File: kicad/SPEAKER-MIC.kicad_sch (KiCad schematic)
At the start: 23 parts, among them J018 SPEAKER1, J18 SPEAKER2, U16 8002D1

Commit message: Added Pi CM4/CM5
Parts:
- removed C16: 1uF, oomwoo_altium:C0402, symbol *:SPEAKER-MIC_0_mirrored_CAP NP_*
- removed C17: 100pF, oomwoo_altium:C0402, symbol *:SPEAKER-MIC_0_CAP NP_*
- removed C5, C93: 0.22uF, oomwoo_altium:CAP-0603, symbol DesignLibrary:SPEAKER-MIC_0_Capacitor-1_DesignLibrary.SchLib
- removed ED1, ED2: ESD5451N, oomwoo_altium:ESD0402, symbol *:SPEAKER-MIC_3_DIODE BI_DIR TRIG_*
- removed MIC1: MIC-4020, oomwoo_altium:MIC-SMD_BD4.0-4013_SMDA, symbol *:SPEAKER-MIC_0_MIC_*
- removed R118, R35: 22K, oomwoo_altium:RES-0402, symbol DesignLibrary:SPEAKER-MIC_0_Resistor-1_DesignLibrary.SchLib
- removed R119: 10K, oomwoo_altium:RES-0402, symbol DesignLibrary:SPEAKER-MIC_1_Resistor-1_DesignLibrary.SchLib
- removed R19: 100R, Resistor_SMD:R_0402_1005Metric, symbol *:SPEAKER-MIC_1_RESISTOR5_*
- removed R21, R22: 1.1K, Resistor_SMD:R_0402_1005Metric, symbol *:SPEAKER-MIC_0_RESISTOR5_*
- added C5: C_Small, symbol Device:C_Small
- added C6, C8: 33n, symbol Device:C_Small
- added C7, C9: 10u, symbol Device:C_Small
- added Q21: RTR030N05HZGTL, LIB_RTR030N05HZGTL:SOT95P280X100-3N, symbol SamacSys_Parts:RTR030N05HZGTL
- added R12, R9: 0, symbol Device:R_US
- added R13, R8: 100k, symbol Device:R_US
- added R2, R6: 270, symbol Device:R_US
- added R5, R7: 150, symbol Device:R_US
- added U11: MAX98357AETE_T, JLCImport:MAX98357AETE_T, symbol JLCImport:MAX98357AETE_T
- added U9: ICS-43434_C5656610, JLCImport:ICS-43434_C5656610, symbol JLCImport:ICS-43434_C5656610
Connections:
- net AUDIO-HP-L: now also R6.1
- net AUDIO-HP-R: now also R2.1
- net GND: now also C5.2, C6.2, C8.2, Q21.2 (S), R12.1, R5.1, R7.1, R8.2, U11.11 (GND), U11.15 (GND), U11.17 (EP), U11.3 (GND), U9.2 (LR), U9.3 (GND)
- net at R36.2, U16.3 (+IN): now also C7.2
- net at R117.1, U16.4 (-IN): now also C9.2
- net AUDIO-SD renamed SP_SHUTDOWN
- net SP_SHUTDOWN: now also Q21.1 (G), R13.2
- net SPK_N: no longer names the net of ED3.1, J18.1
- net SPK_N: now also U11.10 (OUTN)
- net SPK_P: no longer names the net of ED4.1, J18.2
- net SPK_P: now also U11.9 (OUTP)
- net VCC-5V-SYS renamed VCC-5V-REG
- net VCC-5V-REG: now also U11.8 (VDD)
- new net: R12.2, U11.2 (GAIN_SLOT)
- new net: C8.1, C9.1, R6.2, R7.2
- new net: C6.1, C7.1, R2.2, R5.2
- new net: Q21.3 (D), R9.1
- new net: R9.2, U11.4 (SD_MODE#)
- new net BCLK: U11.16 (BCLK), U9.4 (SCK)
- new net DIN: U11.1 (DIN)
- new net DOUT: R8.1, U9.6 (SD)
- new net LRCLK: U11.14 (LRCLK), U9.1 (WS)
- new net VCC3V3_SYS: C5.1, R13.1, U9.5 (VDD)
- no-connect marks 3 -> 5
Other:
- note added: "12dB"
- note added: "LEFT CHANNEL SELECT"
- note added: "Microphone Input"
- note removed: "Microphone Input(Differential)"
- moved on the sheet: C94, C95, ED3, ED4, J018, J18, L3, R117, R36, U16

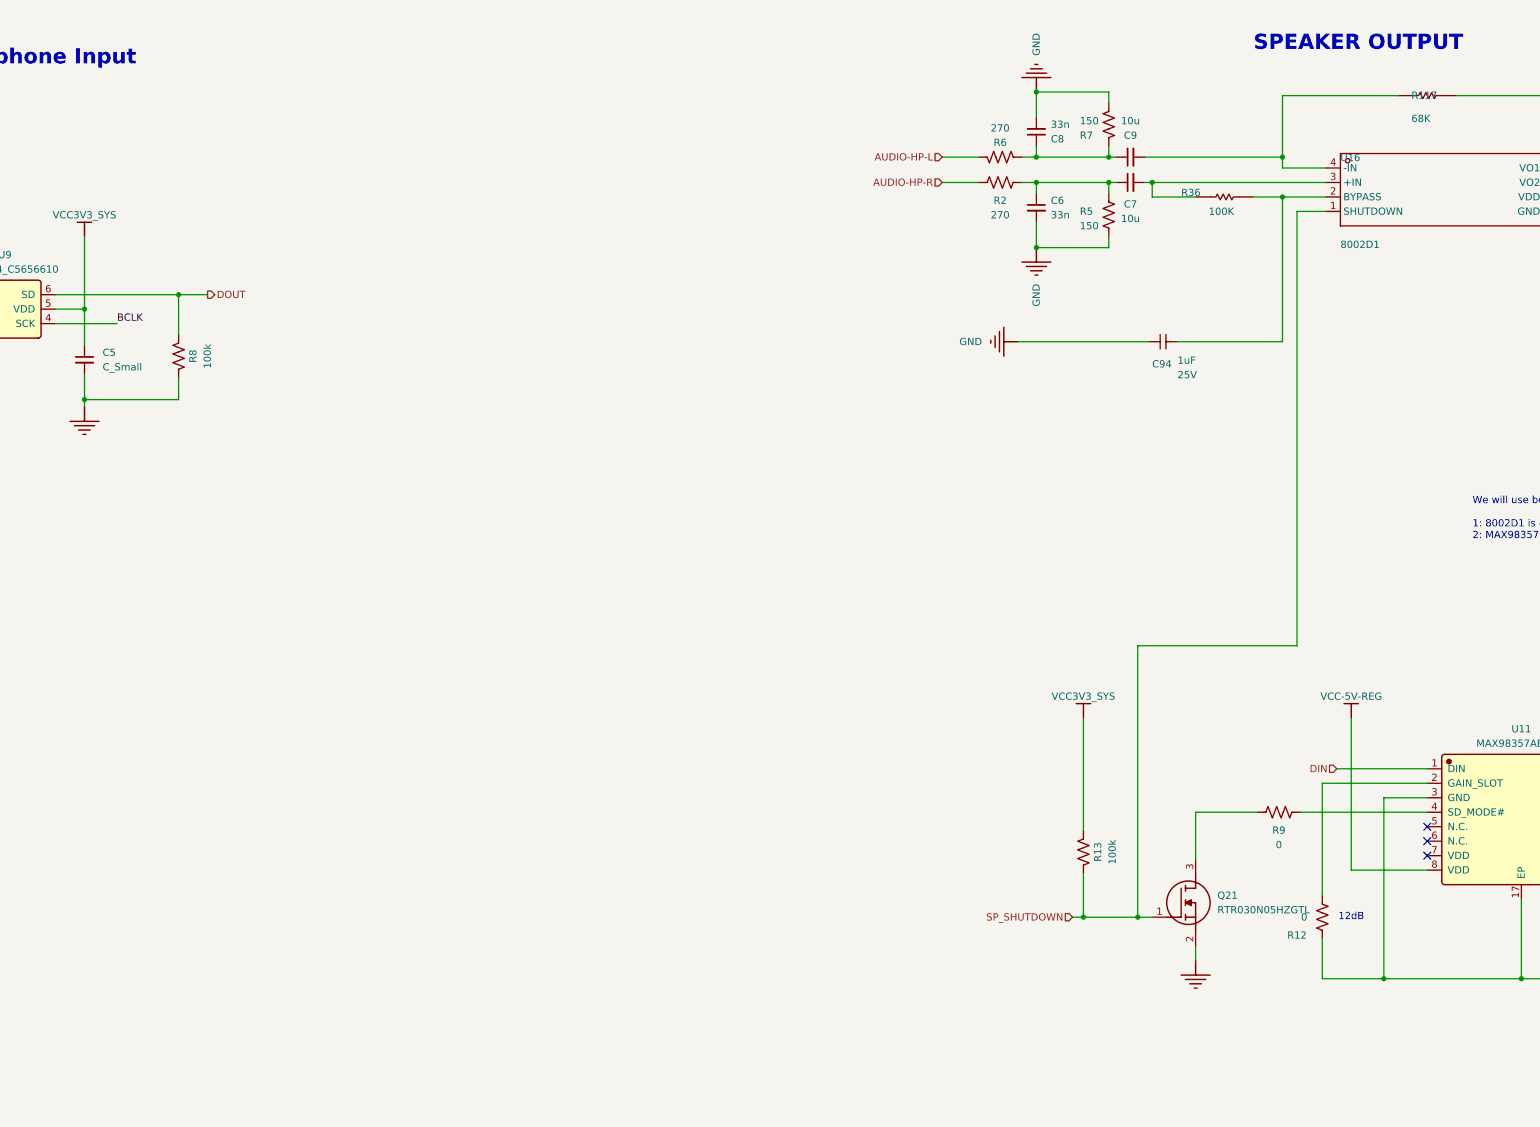
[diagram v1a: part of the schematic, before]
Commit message: Changed MCU to STM32G473VCT6
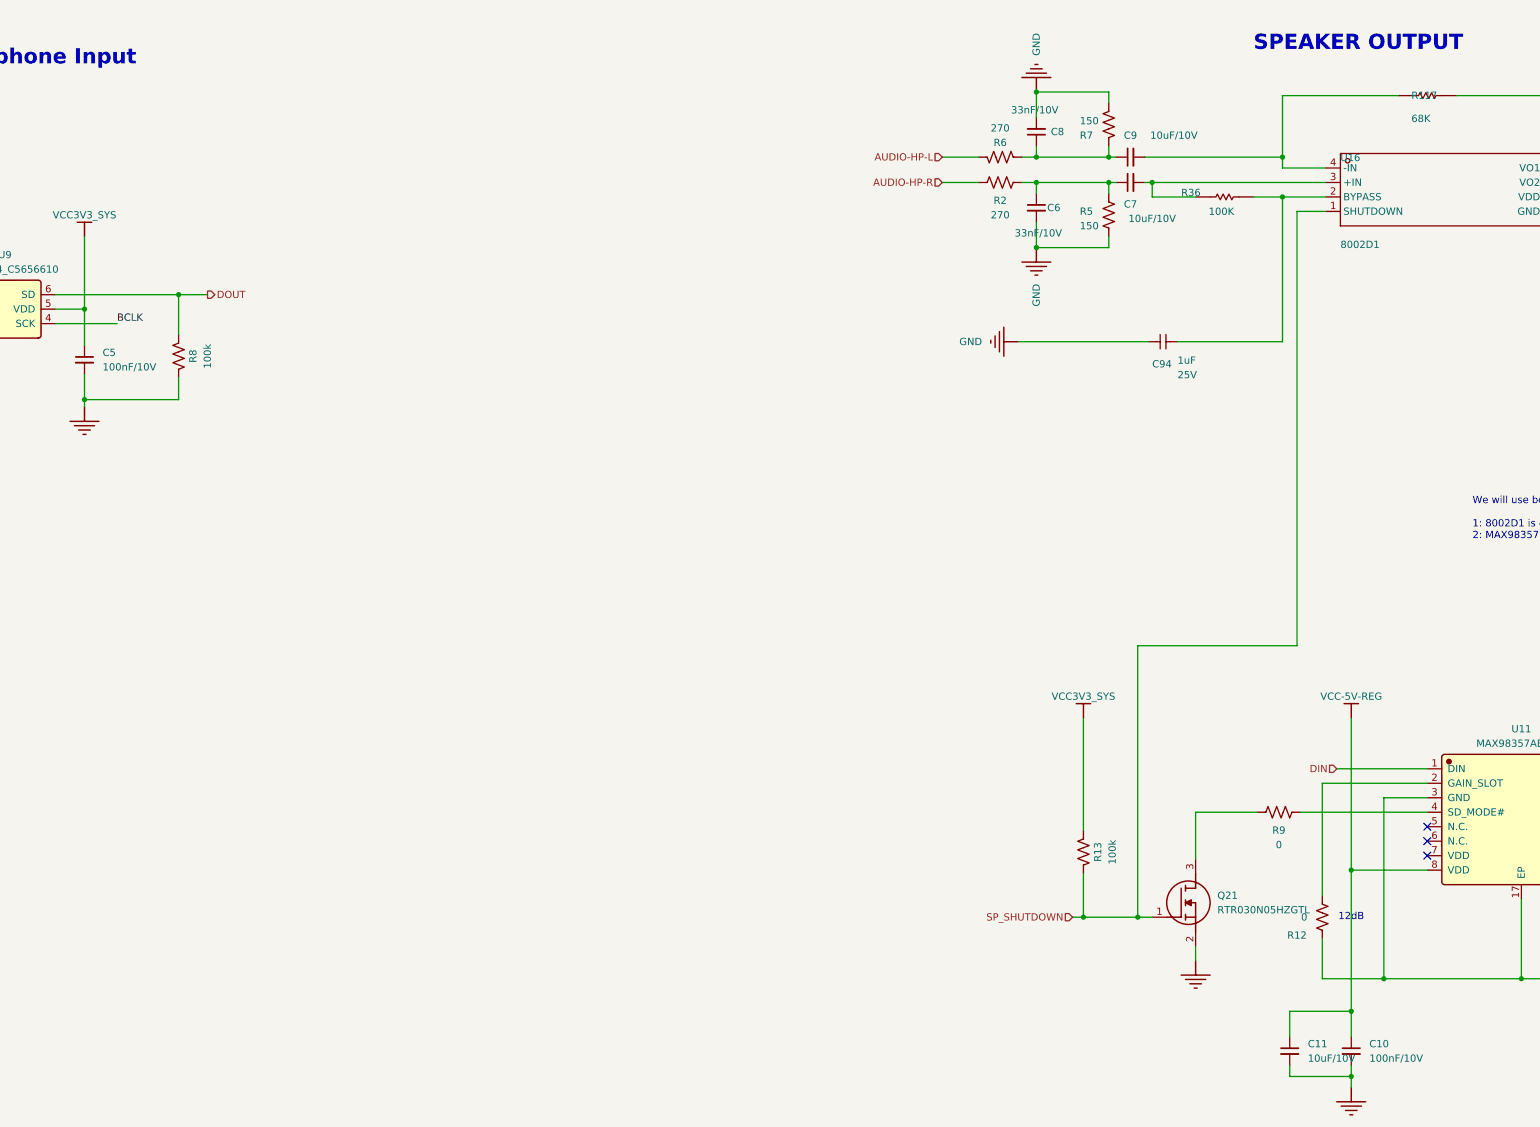
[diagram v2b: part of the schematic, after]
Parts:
- added C10: 100nF/10V, Capacitor_SMD:C_0603_1608Metric, symbol Device:C_Small
- added C11: 10uF/10V, Capacitor_SMD:C_0603_1608Metric, symbol Device:C_Small
- C5: value C_Small -> 100nF/10V; footprint (none) -> Capacitor_SMD:C_0603_1608Metric
- C6, C8: value 33n -> 33nF/10V; footprint (none) -> Capacitor_SMD:C_0603_1608Metric
- C7, C9: value 10u -> 10uF/10V; footprint (none) -> Capacitor_SMD:C_0603_1608Metric
- R12, R13, R2, R5, R6, R7, R8, R9: footprint (none) -> Resistor_SMD:R_0603_1608Metric
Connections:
- net GND: now also C10.2, C11.2
- net VCC-5V-REG: now also C10.1, C11.1

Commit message: STM32G473VCT6
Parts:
- removed C6, C8: 33nF/10V, Capacitor_SMD:C_0603_1608Metric, symbol Device:C_Small
- removed C7: 10uF/10V, Capacitor_SMD:C_0603_1608Metric, symbol Device:C_Small
- removed C94: 1uF, oomwoo_altium:CAP-0402, symbol DesignLibrary:SPEAKER-MIC_0_Capacitor-1_DesignLibrary.SchLib
- removed C95: 10uF, oomwoo_altium:CAP-0402, symbol DesignLibrary:SPEAKER-MIC_0_Capacitor-1_DesignLibrary.SchLib
- removed J018: SPEAKER1, oomwoo_altium:CONN-SMD_2P-P1.00_HX-1.0-2P-WT, symbol DesignLibrary:SPEAKER-MIC_0_HDRx2_DesignLibrary.SchLib
- removed L3: 180R-100M, symbol DesignLibrary:SPEAKER-MIC_0_INDUCTOR-SMD_DesignLibrary.SchLib
- removed Q21: RTR030N05HZGTL, LIB_RTR030N05HZGTL:SOT95P280X100-3N, symbol SamacSys_Parts:RTR030N05HZGTL
- removed R117: 68K, oomwoo_altium:RES-0402, symbol DesignLibrary:SPEAKER-MIC_0_Resistor-1_DesignLibrary.SchLib
- removed R2, R6: 270, Resistor_SMD:R_0603_1608Metric, symbol Device:R_US
- removed R36: 100K, oomwoo_altium:RES-0402, symbol DesignLibrary:SPEAKER-MIC_2_Resistor-1_DesignLibrary.SchLib
- removed R5, R7: 150, Resistor_SMD:R_0603_1608Metric, symbol Device:R_US
- removed U16: 8002D1, oomwoo_altium:SOP-8_L4.9-W3.9-P1.27-LS6.0-BL-1, symbol DesignLibrary:SPEAKER-MIC_0_8002D1_DesignLibrary.SchLib
- added Q14: IRLML6344TRPBF, JLCImport:IRLML6344TRPBF, symbol JLCImport:IRLML6344TRPBF
- added U10: ICS-43434_C5656610, JLCImport:ICS-43434_C5656610, symbol JLCImport:ICS-43434_C5656610
- C9: value 10uF/10V -> 100nF/10V
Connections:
- net BCLK: now also U10.4 (SCK)
- net DOUT: now also U10.6 (SD)
- net GND: now also C9.2, Q14.2 (S), U10.3 (GND)
- net LRCLK: now also U10.1 (WS)
- net SP_SHUTDOWN: now also Q14.1 (G)
- net VCC-5V-REG: now also U11.7 (VDD)
- net VCC-3V3-P: now reaches C9.1
- net VCC-3V3-P: now also C5.1, U9.5 (VDD), U10.2 (LR), U10.5 (VDD)
- net at R9.1: now also Q14.3 (D)
- removed net VCC3V3_SYS: C5.1, R13.1, U9.5 (VDD)
- new net +3.3VP: R13.1
- no-connect marks 5 -> 4
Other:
- note added: "RIGHT CHANNEL SELECT"
- note removed: "SPEAKER OUTPUT"
- moved on the sheet: C10, C11, ED3, ED4, J18, R12, R13, R9, U11
